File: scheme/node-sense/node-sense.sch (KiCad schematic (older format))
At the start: 20 parts, among them P1 Power, P10 CN, P11 CN, P12 CN, P13 CN, P2 CN, P3 CN, P4 CN, P6 CN, P8 CN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

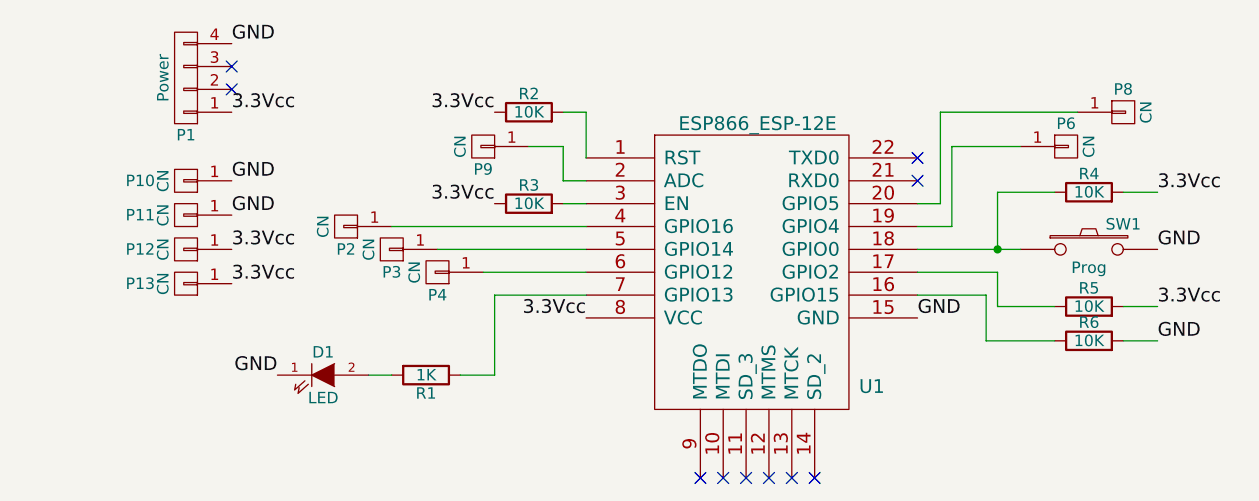
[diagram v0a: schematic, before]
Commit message: node-sene: add more GND/Vcc pads, move tracks to front layer
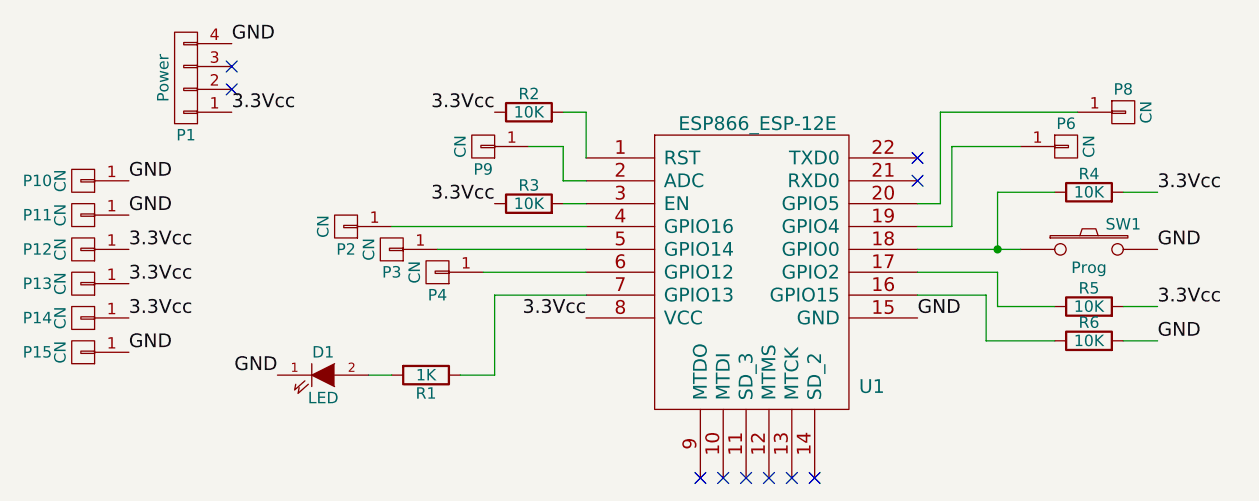
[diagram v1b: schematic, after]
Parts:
- added P14, P15: CN, Pin_Headers:Pin_Header_Straight_1x01, symbol CONN_01X01
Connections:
- net 3.3Vcc: now also P14.1 (P1)
- net GND: now also P15.1 (P1)
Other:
- moved on the sheet: P10, P11, P12, P13
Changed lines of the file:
@@
 L CONN_01X01 P10
 U 1 1 577F9723
-P 1500 2250
-F 0 "P10" H 1700 2250 50  0000 C CNN
-F 1 "CN" V 1600 2250 50  0000 C CNN
-F 2 "Pin_Headers:Pin_Header_Straight_1x01" H 1500 2250 50  0001 C CNN
-F 3 "" H 1500 2250 50  0000 C CNN
-	1    1500 2250
+P 1050 2250
+F 0 "P10" H 1250 2250 50  0000 C CNN
+F 1 "CN" V 1150 2250 50  0000 C CNN
+F 2 "Pin_Headers:Pin_Header_Straight_1x01" H 1050 2250 50  0001 C CNN
+F 3 "" H 1050 2250 50  0000 C CNN
+	1    1050 2250
 	-1   0    0    1
 $EndComp
@@
 L CONN_01X01 P11
 U 1 1 577F97B4
-P 1500 2400
-F 0 "P11" H 1700 2400 50  0000 C CNN
-F 1 "CN" V 1600 2400 50  0000 C CNN
-F 2 "Pin_Headers:Pin_Header_Straight_1x01" H 1500 2400 50  0001 C CNN
-F 3 "" H 1500 2400 50  0000 C CNN
-	1    1500 2400
+P 1050 2400
+F 0 "P11" H 1250 2400 50  0000 C CNN
+F 1 "CN" V 1150 2400 50  0000 C CNN
+F 2 "Pin_Headers:Pin_Header_Straight_1x01" H 1050 2400 50  0001 C CNN
+F 3 "" H 1050 2400 50  0000 C CNN
+	1    1050 2400
 	-1   0    0    1
 $EndComp
@@
 L CONN_01X01 P12
 U 1 1 577F9812
-P 1500 2550
-F 0 "P12" H 1700 2550 50  0000 C CNN
-F 1 "CN" V 1600 2550 50  0000 C CNN
-F 2 "Pin_Headers:Pin_Header_Straight_1x01" H 1500 2550 50  0001 C CNN
-F 3 "" H 1500 2550 50  0000 C CNN
-	1    1500 2550
+P 1050 2550
+F 0 "P12" H 1250 2550 50  0000 C CNN
+F 1 "CN" V 1150 2550 50  0000 C CNN
+F 2 "Pin_Headers:Pin_Header_Straight_1x01" H 1050 2550 50  0001 C CNN
+F 3 "" H 1050 2550 50  0000 C CNN
+	1    1050 2550
 	-1   0    0    1
 $EndComp
@@
 L CONN_01X01 P13
 U 1 1 577F9869
-P 1500 2700
-F 0 "P13" H 1700 2700 50  0000 C CNN
-F 1 "CN" V 1600 2700 50  0000 C CNN
-F 2 "Pin_Headers:Pin_Header_Straight_1x01" H 1500 2700 50  0001 C CNN
-F 3 "" H 1500 2700 50  0000 C CNN
-	1    1500 2700
+P 1050 2700
+F 0 "P13" H 1250 2700 50  0000 C CNN
+F 1 "CN" V 1150 2700 50  0000 C CNN
+F 2 "Pin_Headers:Pin_Header_Straight_1x01" H 1050 2700 50  0001 C CNN
+F 3 "" H 1050 2700 50  0000 C CNN
+	1    1050 2700
 	-1   0    0    1
 $EndComp
-Text Label 1700 2250 0    60   ~ 0
+Text Label 1250 2250 0    60   ~ 0
 GND
-Text Label 1700 2400 0    60   ~ 0
+Text Label 1250 2400 0    60   ~ 0
 GND
-Text Label 1700 2700 0    60   ~ 0
+Text Label 1250 2700 0    60   ~ 0
 3.3Vcc
 NoConn ~ 4700 2150
 NoConn ~ 4700 2250
-Text Label 1700 2550 0    60   ~ 0
+Text Label 1250 2550 0    60   ~ 0
 3.3Vcc
+$Comp
+L CONN_01X01 P14
+U 1 1 578CBA12
+P 1050 2850
+F 0 "P14" H 1250 2850 50  0000 C CNN
+F 1 "CN" V 1150 2850 50  0000 C CNN
+F 2 "Pin_Headers:Pin_Header_Straight_1x01" H 1050 2850 50  0001 C CNN
+F 3 "" H 1050 2850 50  0000 C CNN
+	1    1050 2850
+	-1   0    0    1
+$EndComp
+Text Label 1250 2850 0    60   ~ 0
+3.3Vcc
+$Comp
+L CONN_01X01 P15
+U 1 1 578CBE3B
+P 1050 3000
+F 0 "P15" H 1250 3000 50  0000 C CNN
+F 1 "CN" V 1150 3000 50  0000 C CNN
+F 2 "Pin_Headers:Pin_Header_Straight_1x01" H 1050 3000 50  0001 C CNN
+F 3 "" H 1050 3000 50  0000 C CNN
+	1    1050 3000
+	-1   0    0    1
+$EndComp
+Text Label 1250 3000 0    60   ~ 0
+GND
 $EndSCHEMATC
